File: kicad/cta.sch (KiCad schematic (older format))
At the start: 23 parts, among them Q1 TIP120, Q2 KSP2907, U1 LM324

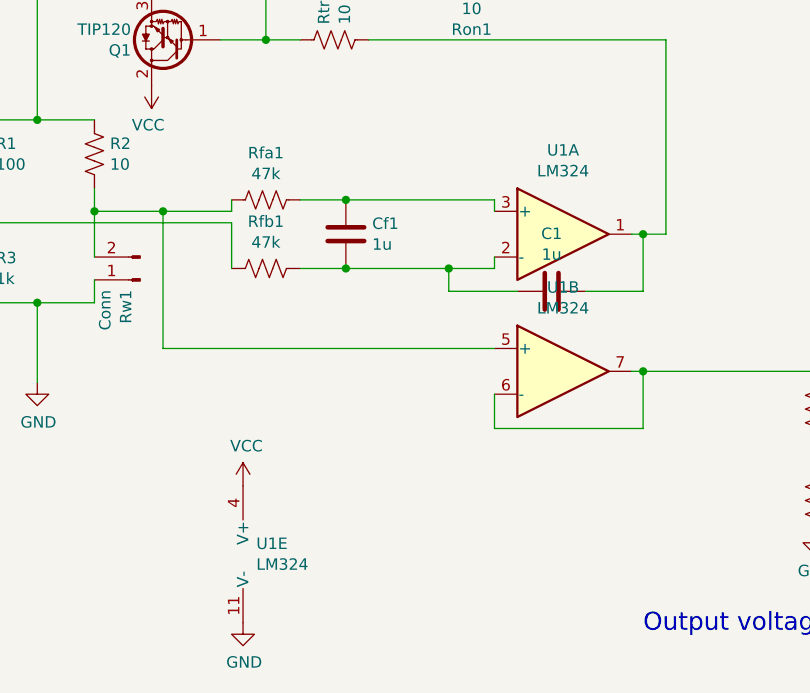
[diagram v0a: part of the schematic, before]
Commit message: Added a decoupling capacitor to op amp and improved layout
I don't know if this will help but it may reduce noise and improve performance when voltage input is noisy.
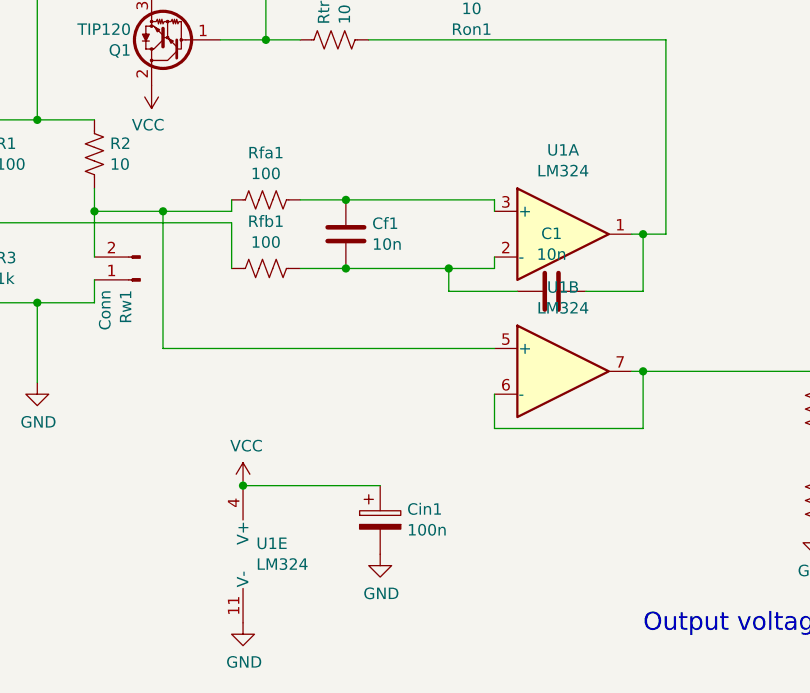
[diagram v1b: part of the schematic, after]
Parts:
- added Cin1: 100n, Capacitor_THT:CP_Radial_D4.0mm_P2.00mm, symbol Device:CP
- C1, Cf1: value 1u -> 10n
- Rfa1, Rfb1: value 47k -> 100
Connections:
- net GND: now also Cin1.2
- net VCC: now also Cin1.1
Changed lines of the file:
@@
 P 3750 2850
 F 0 "Rfa1" V 3545 2850 50  0000 C CNN
-F 1 "47k" V 3636 2850 50  0000 C CNN
+F 1 "100" V 3636 2850 50  0000 C CNN
 F 2 "Resistor_THT:R_Axial_DIN0207_L6.3mm_D2.5mm_P10.16mm_Horizontal" V 3790 2840 50  0001 C CNN
 F 3 "~" H 3750 2850 50  0001 C CNN
@@
 P 3750 3150
 F 0 "Rfb1" V 3545 3150 50  0000 C CNN
-F 1 "47k" V 3636 3150 50  0000 C CNN
+F 1 "100" V 3636 3150 50  0000 C CNN
 F 2 "Resistor_THT:R_Axial_DIN0207_L6.3mm_D2.5mm_P10.16mm_Horizontal" V 3790 3140 50  0001 C CNN
 F 3 "~" H 3750 3150 50  0001 C CNN
@@
 P 4100 3000
 F 0 "Cf1" H 4215 3046 50  0000 L CNN
-F 1 "1u" H 4215 2955 50  0000 L CNN
+F 1 "10n" H 4215 2955 50  0000 L CNN
 F 2 "Capacitor_THT:C_Rect_L7.2mm_W4.5mm_P5.00mm_FKS2_FKP2_MKS2_MKP2" H 4138 2850 50  0001 C CNN
 F 3 "~" H 4100 3000 50  0001 C CNN
@@
 P 5000 3250
 F 0 "C1" V 4748 3250 50  0000 C CNN
-F 1 "1u" V 4839 3250 50  0000 C CNN
+F 1 "10n" V 4839 3250 50  0000 C CNN
 F 2 "Capacitor_THT:C_Rect_L7.2mm_W4.5mm_P5.00mm_FKS2_FKP2_MKS2_MKP2" H 5038 3100 50  0001 C CNN
 F 3 "~" H 5000 3250 50  0001 C CNN
@@
 Wire Wire Line
 	8950 4050 9100 4050
+$Comp
+L Device:CP Cin1
+U 1 1 5FE3B35B
+P 4250 4250
+F 0 "Cin1" H 4368 4296 50  0000 L CNN
+F 1 "100n" H 4368 4205 50  0000 L CNN
+F 2 "Capacitor_THT:CP_Radial_D4.0mm_P2.00mm" H 4288 4100 50  0001 C CNN
+F 3 "~" H 4250 4250 50  0001 C CNN
+	1    4250 4250
+	1    0    0    -1
+$EndComp
+$Comp
+L power:GND #PWR0114
+U 1 1 5FE3C993
+P 4250 4400
+F 0 "#PWR0114" H 4250 4150 50  0001 C CNN
+F 1 "GND" H 4255 4227 50  0000 C CNN
+F 2 "" H 4250 4400 50  0001 C CNN
+F 3 "" H 4250 4400 50  0001 C CNN
+	1    4250 4400
+	1    0    0    -1
+$EndComp
+Wire Wire Line
+	3650 4100 4250 4100
+Connection ~ 3650 4100
 $EndSCHEMATC
